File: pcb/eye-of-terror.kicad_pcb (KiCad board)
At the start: 4 copper layers, 200 x 200 mm, 226 parts, among them J1 Conn_01x02_Socket, J2 G-Switch GT-USB-7055E, J3 Conn_01x04, J4 Conn_01x04, J5 Conn_01x03, J6 Conn_01x02_Socket, J7 Conn_01x02_Socket, J8 Conn_01x03, Q1 IPT020N10N3, Q10 ALS-PT19-315C/L177/TR8, Q11 ALS-PT19-315C/L177/TR8, Q12 ALS-PT19-315C/L177/TR8, Q13 ALS-PT19-315C/L177/TR8, Q14 ALS-PT19-315C/L177/TR8, Q15 ALS-PT19-315C/L177/TR8, Q16 ALS-PT19-315C/L177/TR8, Q17 ALS-PT19-315C/L177/TR8, Q2 IPT020N10N3, Q3 IPT020N10N3, Q4 IPT020N10N3, Q5 IPT020N10N3, Q6 IPT020N10N3, Q7 ALS-PT19-315C/L177/TR8, Q8 ALS-PT19-315C/L177/TR8, Q9 ALS-PT19-315C/L177/TR8, SW1 SW_Push, SW2 SW_Push, U1 RP2350B, U2 TD1660, U3 AP63205WU-7, U4 LSM6DS3, U5 W25Q32JVSS, U7 DRV8353HRTAR, Y1 ABM8-272-T3

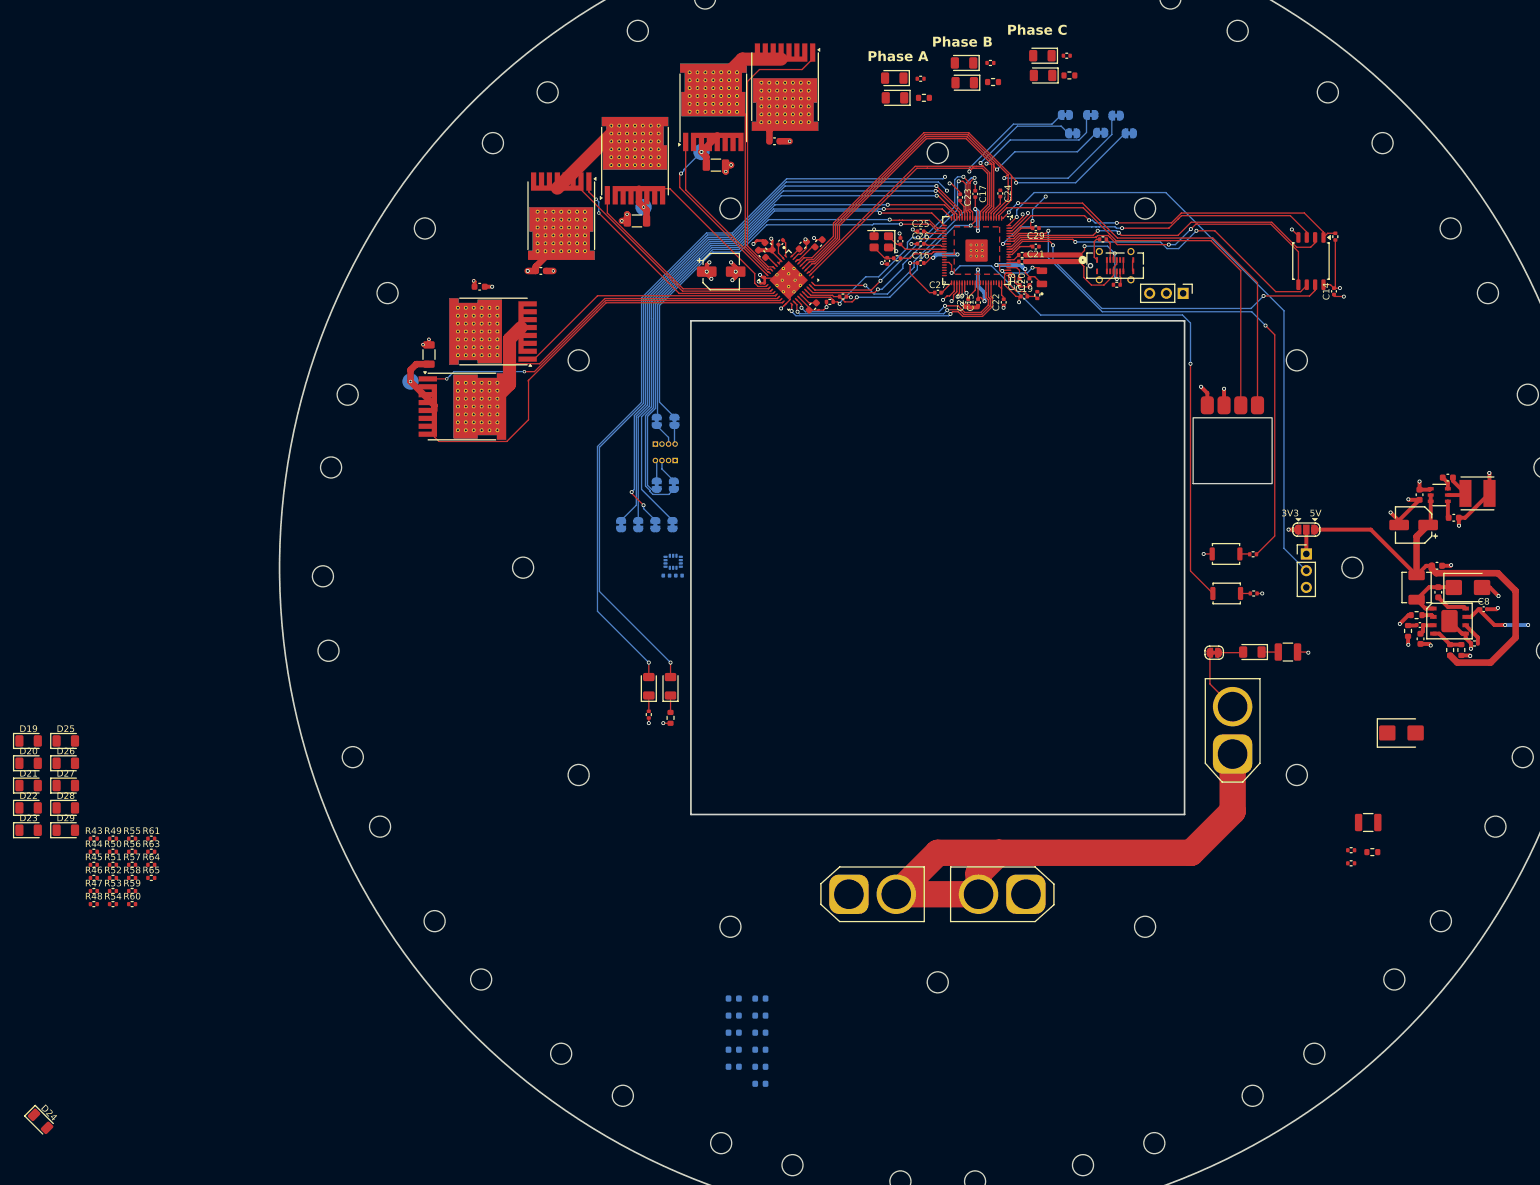
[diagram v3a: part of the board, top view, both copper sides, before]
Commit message: fixing DRC errors.
routing and placement done.
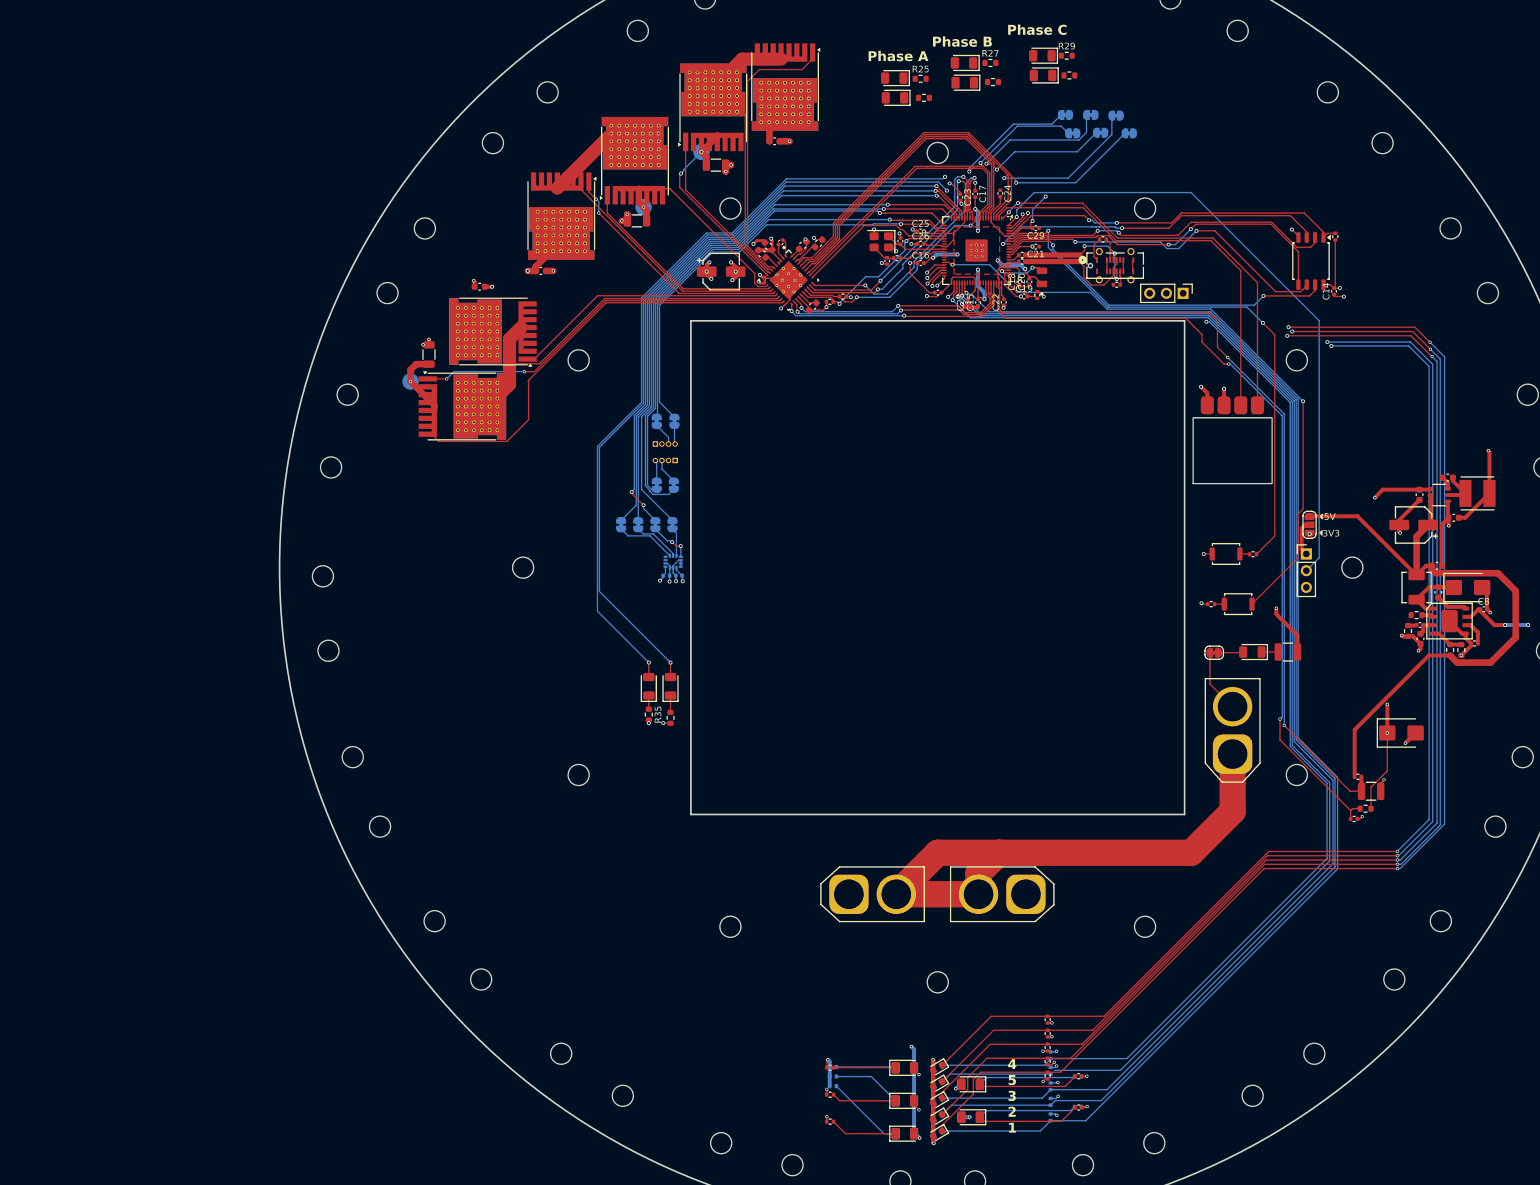
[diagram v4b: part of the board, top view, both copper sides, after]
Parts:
- removed D29: RED, Diode_SMD:D_1206_3216Metric
- removed Q17: ALS-PT19-315C/L177/TR8, LED_SMD:LED_0603_1608Metric
- removed R61: 68, Resistor_SMD:R_0402_1005Metric
- removed R65: 10k, Resistor_SMD:R_0402_1005Metric
- D24, D25, D26, D27, D28, R52, R53, R54, R56, R57, R58, R59, R60, R63, R64: moved to B.Cu
- Q10, Q11, Q7, Q8, Q9: moved to F.Cu
- R25, R27, R29, R35: value 68 -> 15; footprint Resistor_SMD:R_0402_1005Metric -> Resistor_SMD:R_0603_1608Metric
- moved R51 151.3 mm to (330.1, 281.1)
- moved R49 151.1 mm to (330.1, 276.4)
- moved D23 149.6 mm to (313.7, 282.6), turned to 180 degrees
- moved R43 149.3 mm to (325.4, 276.2), turned to 90 degrees
- moved D22 149.2 mm to (313.7, 277.6), turned to 180 degrees
- moved R46 147.6 mm to (325.4, 274.1), turned to 90 degrees
- moved R60 147.0 mm to (330.0, 281.0)
- moved R48 146.6 mm to (325.4, 272.0), turned to 90 degrees
- moved R59 146.4 mm to (330.0, 276.4)
- moved D28 145.3 mm to (313.7, 282.6), turned to 180 degrees
- moved D27 144.8 mm to (313.7, 277.6), turned to 180 degrees
- moved R50 144.3 mm to (325.4, 267.8), turned to 90 degrees
- moved D21 143.2 mm to (303.7, 285.1)
- moved R58 143.1 mm to (325.9, 277.9), turned to -90 degrees
- moved R57 143.0 mm to (325.9, 275.5), turned to -90 degrees
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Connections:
- U1 pad 47: /ENC_SENSE_11 -> unconnected-(U1-GPIO38-Pad47)
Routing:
- net /ENC_SENSE_1: track 0.00 -> 255.5 mm, vias 0 -> 4
- net /ENC_SENSE_2: track 0.00 -> 252.0 mm, vias 0 -> 4
- net /ENC_SENSE_3: track 0.00 -> 249.1 mm, vias 0 -> 4
- net /ENC_SENSE_5: track 0.00 -> 243.4 mm, vias 0 -> 3
- net /ENC_SENSE_4: track 0.00 -> 242.4 mm, vias 0 -> 3
- net /ENC_SENSE_10: track 1.65 -> 209.1 mm
- net /ENC_SENSE_9: track 1.96 -> 207.9 mm
- net /ENC_SENSE_8: track 2.24 -> 206.8 mm
- net /ENC_SENSE_7: track 3.13 -> 205.0 mm
- net /ENC_SENSE_6: track 3.54 -> 205.0 mm, vias 1 -> 2
- net +BATT: track 46.2 -> 235.5 mm, vias 9 -> 10
- net /BATT_MON: track 0.00 -> 122.4 mm, vias 0 -> 2
- net /5V_MON: track 0.00 -> 121.8 mm, vias 0 -> 2
- net +3V3: track 71.7 -> 141.0 mm, vias 10 -> 33
- net DGND: track 52.2 -> 105.4 mm, vias 22 -> 33
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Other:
- board text added: "4 5 3 2 1"
- board text added: "6 7 8 9 10"

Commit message: WIP version 2
* (tried to) remove backup files from repo
* increased current-limiting resistors on green and blue LEDs
* added pins for motor windings
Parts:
- removed R20: 68k, Resistor_SMD:R_0603_1608Metric
- removed R21: 10k, Resistor_SMD:R_0402_1005Metric
- removed R22: 1k, Resistor_SMD:R_0402_1005Metric
- removed R23: 1.5k, Resistor_SMD:R_1210_3225Metric
- added NT1: NetTie_2, NetTie:NetTie-2_SMD_Pad2.0mm, F.Cu at (376.5, 181.5)
- added NT2: NetTie_2, NetTie:NetTie-2_SMD_Pad2.0mm, F.Cu at (176.2, 146.8)
- added TP4: PHASE_U, TestPoint:TestPoint_Pad_D2.5mm, F.Cu at (90.0, 227.1)
- added TP5: PHASE_U, TestPoint:TestPoint_Pad_D2.5mm, F.Cu at (90.0, 231.6)
- added TP6: PHASE_V, TestPoint:TestPoint_Pad_D2.5mm, F.Cu at (170.4, 147.6)
- added TP7: PHASE_V, TestPoint:TestPoint_Pad_D2.5mm, F.Cu at (170.4, 152.1)
- added TP8: PHASE_W, TestPoint:TestPoint_Pad_D2.5mm, F.Cu at (170.4, 156.7)
- added TP9: PHASE_W, TestPoint:TestPoint_Pad_D2.5mm, F.Cu at (170.4, 161.2)
- D18: value GREEN -> RED
- R25, R26, R27, R28, R29, R30, R35, R38: value 15 -> 100
- R40: value 1.5k -> 1k
- moved R29 0.45 mm to (328.8, 121.3)
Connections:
- U7 pad 41: PGND -> unconnected-(U7-PAD-Pad41)_5
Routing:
- net PGND: track 201.7 -> 268.8 mm
- net +BATT_RAW: track 85.1 -> 72.6 mm
- net unconnected-(U7-PAD-Pad41)_9: track 0.00 -> 4.51 mm
